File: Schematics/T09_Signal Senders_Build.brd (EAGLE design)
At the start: 88.6 x 64.8 mm, 39 parts, among them IC1 7805TV, IC2 7805TV, IC3 ATMEGA328, SW1 , X1 , Y2 16MHz

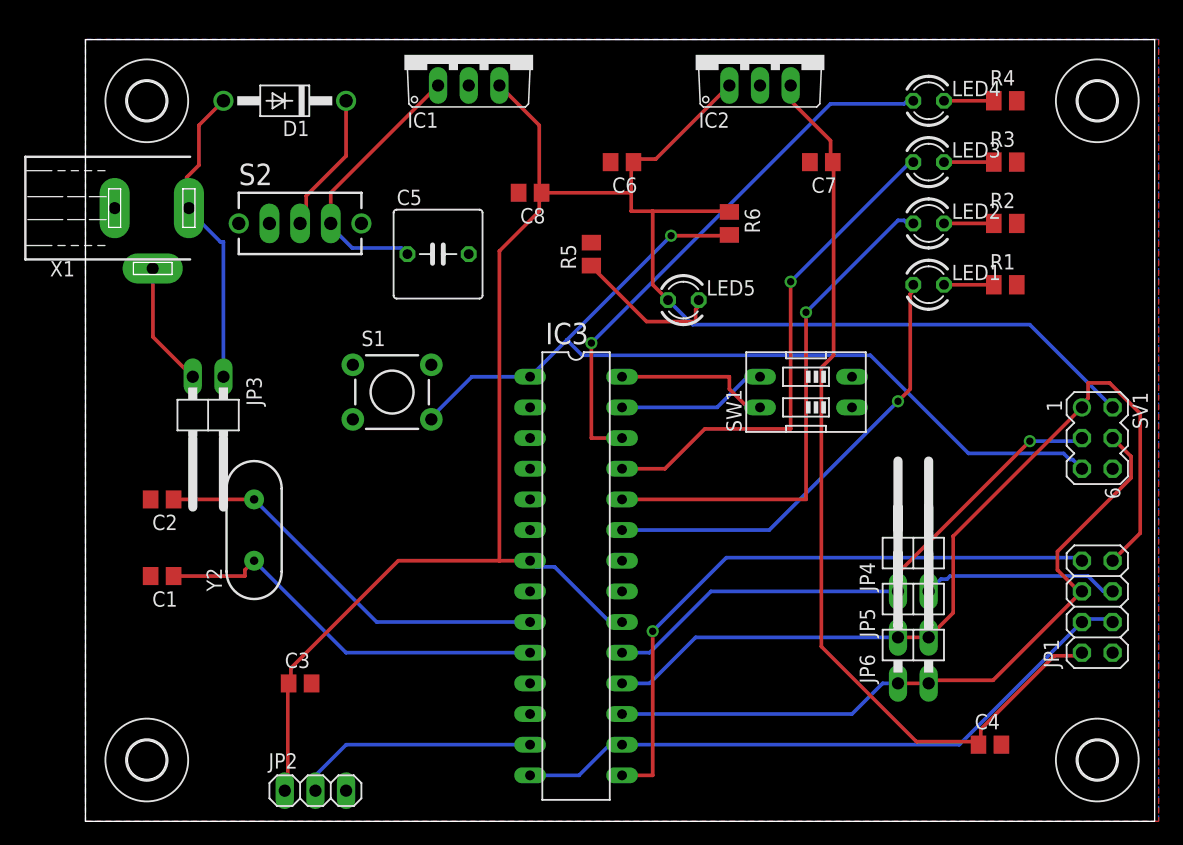
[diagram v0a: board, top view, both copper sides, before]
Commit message: PCB - added vias, added headers to uC unused pins
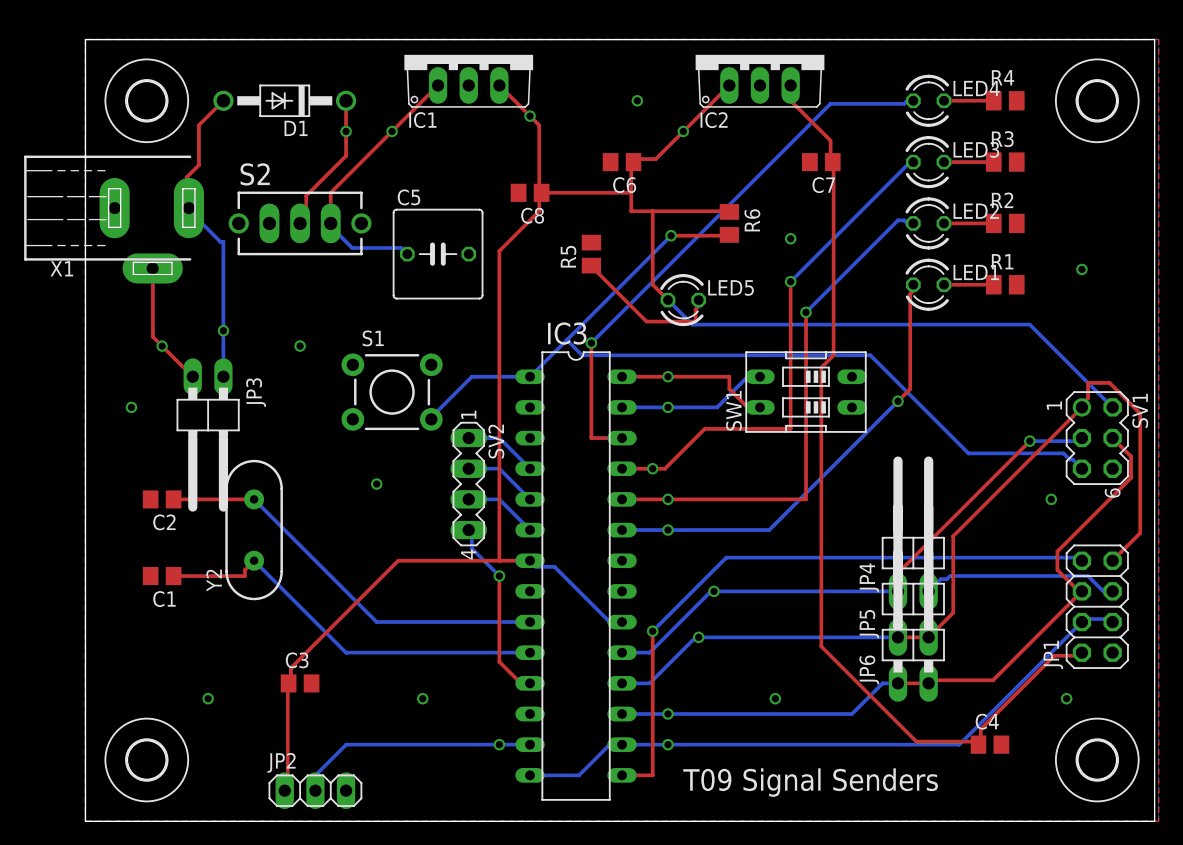
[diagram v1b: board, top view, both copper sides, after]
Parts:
- added SV2: (no value), con-lstb:MA04-1
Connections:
- net N$11: now also SV2.1
- net N$12: now also SV2.2
- net N$15: now also SV2.3
- net N$16: now also SV2.4
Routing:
- net N$16: track 0.00 -> 15.5 mm, vias 0 -> 1
- net N$15: track 0.00 -> 6.13 mm
- net N$12: track 0.00 -> 6.13 mm
- net N$11: track 0.00 -> 6.13 mm
- net N$14: vias 0 -> 1
- net SPI_CE: vias 0 -> 1
- net RF_SPIDSCSC: vias 0 -> 1
- net RF_SPIDSCS: vias 0 -> 1
- net RF_SPI5: vias 1 -> 2
- net N$9: vias 0 -> 1
- net N$4: vias 0 -> 1
- net N$23: vias 0 -> 1
- net N$22: vias 0 -> 1
- net N$10: vias 0 -> 1
- net LED2: vias 1 -> 2
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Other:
- board text added: "Chris Klupenger Max Cope Leslie Eide"
- board text added: "T09 Signal Senders"

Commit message: Fixed Nets. Fixed Silkscreen Layer
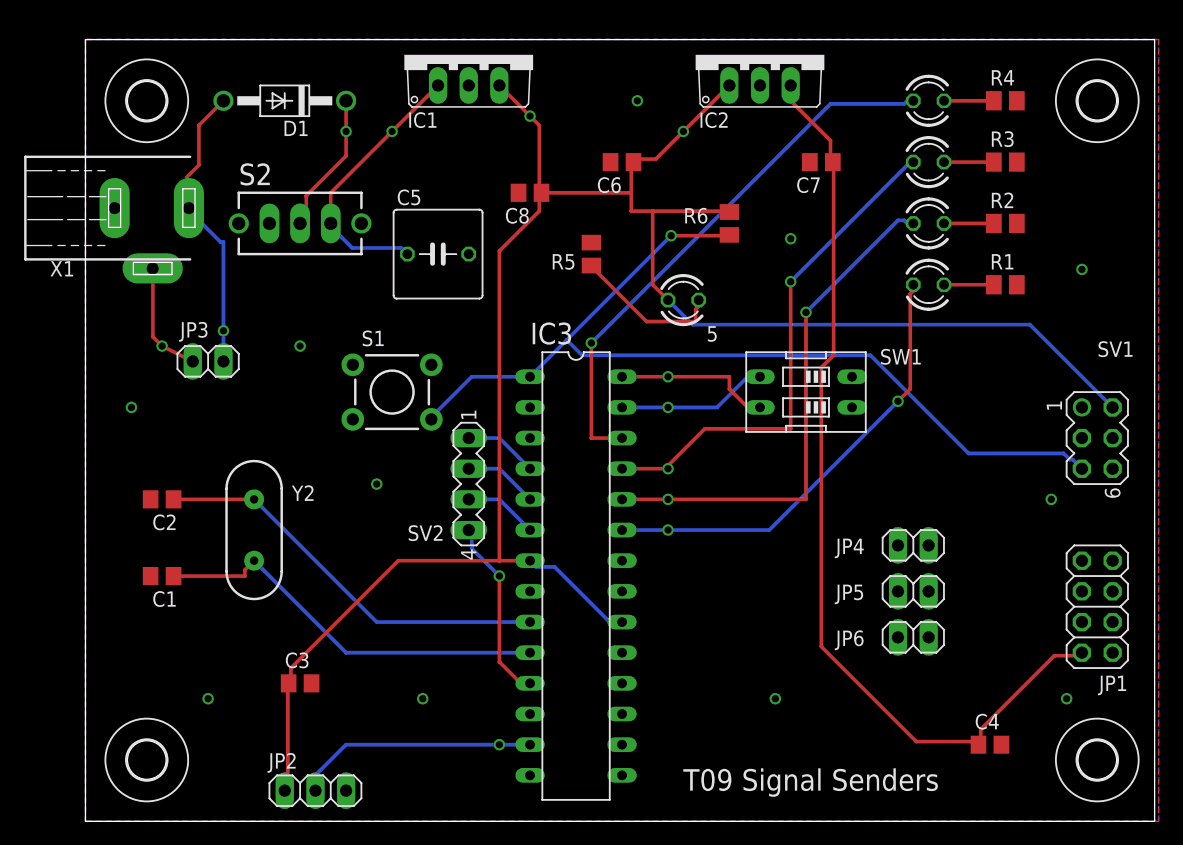
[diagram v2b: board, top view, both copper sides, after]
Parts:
- 5: value RED -> POWER
- JP1: value (none) -> RF
- JP2: value (none) -> IR
- JP3: value (none) -> Battery; device pinhead:1X02/90 -> pinhead:1X02
- JP4, JP5, JP6: device pinhead:1X02/90 -> pinhead:1X02
- LED1: value RED -> WEST
- LED2: value GREEN -> EAST
- LED3: value YELLOW -> SOUTH
- LED4: value BLUE -> NORTH
- S2: value TL32YO -> POWER
- SV1: value (none) -> SPI
- SW1: value (none) -> UNIT_ID
- moved JP3 5.08 mm to (10.2, 38.1)
- renumbered LED5 to 5
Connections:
- net RF_SPDSCSC renamed N$35
- net RF_SPI5 renamed N$33
- net RF_SPIDSCSD renamed N$39
- removed net RF_SPIDSCS: IC3.18, JP1.7, JP5.1, JP5.2, SV1.1
- removed net RF_SPIDSCSC: IC3.17, JP1.6, JP6.1, JP6.2, SV1.4
- removed net SPI_CE: IC3.14, IC3.16, JP1.3, JP1.4
- new net N$31: IC3.17, IC3.18, JP5.1, JP6.1, SV1.1, SV1.4
- new net N$34: IC3.14, JP1.4
- new net N$36: IC3.16, JP1.3
- new net N$37: JP1.6, JP6.2
- new net N$38: JP1.7, JP5.2
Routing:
- net RF_SPIDSCS: track 72.0 -> 0.00 mm, vias 1 -> 0
- net RF_SPIDSCSC: track 59.3 -> 0.00 mm, vias 1 -> 0
- net SPI_CE: track 53.7 -> 0.00 mm, vias 1 -> 0
- net N$35: track 52.7 -> 0.00 mm, vias 1 -> 0
- net N$33: track 46.4 -> 0.00 mm, vias 2 -> 0
- net N$39: track 16.3 -> 0.00 mm
- net +9V: track 25.9 -> 24.6 mm
- net N$14: track 10.3 -> 9.59 mm

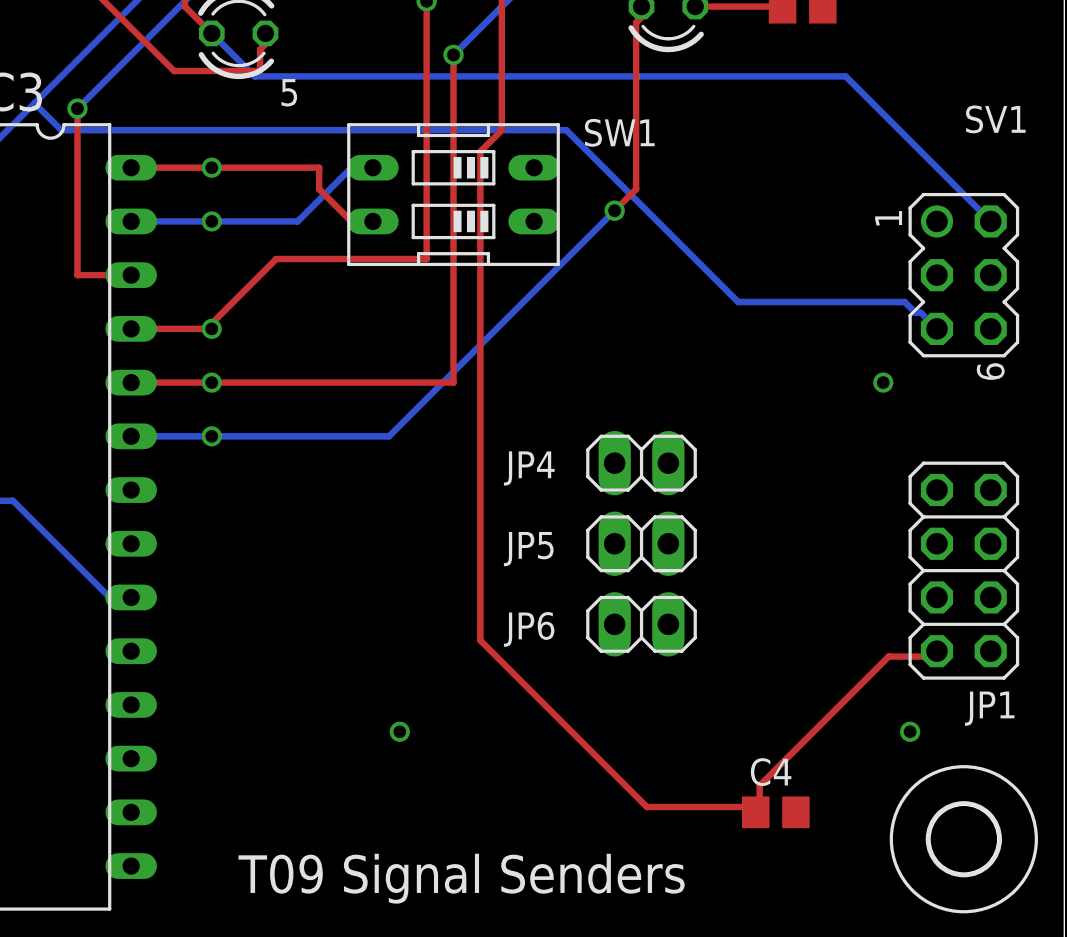
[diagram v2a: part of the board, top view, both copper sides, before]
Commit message: RF nets still had errors. Still need to be routed.
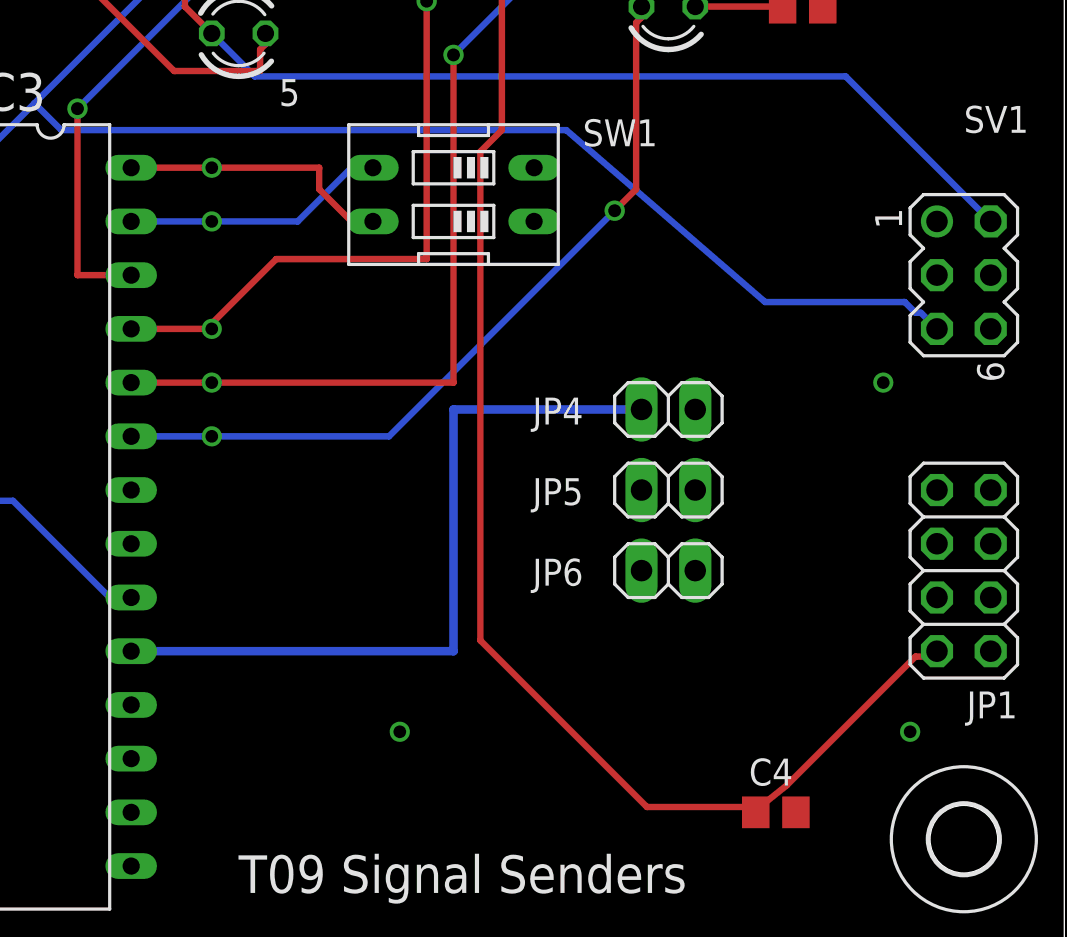
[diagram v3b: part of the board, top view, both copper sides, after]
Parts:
- SV2: value (none) -> (none)
- moved JP6 2.84 mm to (69.8, 17.8)
- moved JP4 2.84 mm to (69.8, 25.4)
- moved JP5 2.84 mm to (69.8, 21.6)
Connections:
- new net N$32: IC3.17, JP6.1, SV1.4
- net N$31: no longer IC3.17, JP6.1, SV1.4
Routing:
- net N$33: track 0.00 -> 35.6 mm
- net +3V3: track 77.9 -> 77.3 mm
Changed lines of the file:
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@@
 <attribute name="NAME" x="60.96" y="53.34" size="1.27" layer="25" rot="R180"/>
 </element>
-<element name="JP4" library="pinhead" package="1X02" value=" " x="68.58" y="22.86" smashed="yes">
-<attribute name="NAME" x="62.1538" y="22.1488" size="1.27" layer="25" ratio="10"/>
-<attribute name="VALUE" x="66.04" y="19.685" size="1.27" layer="27"/>
-</element>
-<element name="JP5" library="pinhead" package="1X02" value=" " x="68.58" y="19.05" smashed="yes">
-<attribute name="NAME" x="62.1538" y="18.3388" size="1.27" layer="25" ratio="10"/>
-<attribute name="VALUE" x="66.04" y="15.875" size="1.27" layer="27"/>
-</element>
-<element name="JP6" library="pinhead" package="1X02" value=" " x="68.58" y="15.24" smashed="yes">
-<attribute name="NAME" x="62.1538" y="14.5288" size="1.27" layer="25" ratio="10"/>
-<attribute name="VALUE" x="66.04" y="12.065" size="1.27" layer="27"/>
+<element name="JP4" library="pinhead" package="1X02" value=" " x="69.85" y="25.4" smashed="yes">
+<attribute name="NAME" x="63.4238" y="24.6888" size="1.27" layer="25" ratio="10"/>
+<attribute name="VALUE" x="67.31" y="22.225" size="1.27" layer="27"/>
+</element>
+<element name="JP5" library="pinhead" package="1X02" value=" " x="69.85" y="21.59" smashed="yes">
+<attribute name="NAME" x="63.4238" y="20.8788" size="1.27" layer="25" ratio="10"/>
+<attribute name="VALUE" x="67.31" y="18.415" size="1.27" layer="27"/>
+</element>
+<element name="JP6" library="pinhead" package="1X02" value=" " x="69.85" y="17.78" smashed="yes">
+<attribute name="NAME" x="63.4238" y="17.0688" size="1.27" layer="25" ratio="10"/>
+<attribute name="VALUE" x="67.31" y="14.605" size="1.27" layer="27"/>
 </element>
 <element name="R6" library="rcl" package="M0805" value="1k" x="53.34" y="49.53" smashed="yes" rot="R270">
@@
 <element name="U$3" library="holes" package="3,2" value="" x="83.82" y="59.69" smashed="yes"/>
 <element name="U$4" library="holes" package="3,2" value="" x="5.08" y="59.69" smashed="yes"/>
-<element name="SV2" library="con-lstb" package="MA04-1" value="" x="31.75" y="27.94" smashed="yes" rot="R270">
+<element name="SV2" library="con-lstb" package="MA04-1" value=" " x="31.75" y="27.94" smashed="yes" rot="R270">
 <attribute name="OC_NEWARK" value="unknown" x="31.75" y="27.94" size="1.778" layer="27" rot="R270" display="off"/>
 <attribute name="MPN" value="" x="31.75" y="27.94" size="1.778" layer="27" rot="R270" display="off"/>
@@
 <wire x1="81.534" y1="29.972" x2="81.788" y2="29.972" width="0.3048" layer="16"/>
 <wire x1="81.026" y1="30.48" x2="81.534" y2="29.972" width="0.3048" layer="16"/>
-<wire x1="73.152" y1="30.48" x2="81.026" y2="30.48" width="0.3048" layer="16"/>
-<wire x1="65.024" y1="38.608" x2="73.152" y2="30.48" width="0.3048" layer="16"/>
+<wire x1="74.422" y1="30.48" x2="81.026" y2="30.48" width="0.3048" layer="16"/>
+<wire x1="65.024" y1="38.608" x2="74.422" y2="30.48" width="0.3048" layer="16"/>
 <wire x1="41.148" y1="38.608" x2="65.024" y2="38.608" width="0.3048" layer="16"/>
 <wire x1="39.878" y1="39.878" x2="41.148" y2="38.608" width="0.3048" layer="16"/>
@@
 <wire x1="58.42" y1="60.96" x2="58.42" y2="59.69" width="0.3048" layer="1"/>
 <wire x1="61.722" y1="54.61" x2="61.91" y2="54.61" width="0.3048" layer="1"/>
-<wire x1="74.168" y1="7.62" x2="74.168" y2="6.604" width="0.3048" layer="1"/>
+<wire x1="75.438" y1="7.62" x2="74.168" y2="6.604" width="0.3048" layer="1"/>
 <wire x1="74.168" y1="6.604" x2="74.168" y2="6.35" width="0.3048" layer="1"/>
-<wire x1="80.264" y1="13.716" x2="74.168" y2="7.62" width="0.3048" layer="1"/>
-<wire x1="82.55" y1="13.716" x2="80.264" y2="13.716" width="0.3048" layer="1"/>
+<wire x1="81.534" y1="13.716" x2="75.438" y2="7.62" width="0.3048" layer="1"/>
+<wire x1="82.55" y1="13.716" x2="81.534" y2="13.716" width="0.3048" layer="1"/>
 <wire x1="82.55" y1="13.97" x2="82.55" y2="13.716" width="0.3048" layer="1"/>
 <wire x1="74.168" y1="6.35" x2="73.98" y2="6.35" width="0.3048" layer="1"/>
@@
 <via x="58.42" y="48.26" extent="1-16" drill="0.6"/>
 </signal>
-<signal name="N$31">
-<contactref element="IC3" pad="17"/>
-<contactref element="SV1" pad="4"/>
-<contactref element="JP6" pad="1"/>
-<contactref element="IC3" pad="18"/>
-<contactref element="SV1" pad="1"/>
-<contactref element="JP5" pad="1"/>
-<wire x1="82.55" y1="34.29" x2="85.09" y2="31.75" width="0" layer="19" extent="1-1"/>
-<wire x1="67.31" y1="19.05" x2="85.09" y2="31.75" width="0" layer="19" extent="1-1"/>
-<wire x1="67.31" y1="15.24" x2="67.31" y2="19.05" width="0" layer="19" extent="1-1"/>
-<wire x1="44.45" y1="11.43" x2="67.31" y2="15.24" width="0" layer="19" extent="1-1"/>
-<wire x1="44.45" y1="8.89" x2="44.45" y2="11.43" width="0" layer="19" extent="1-1"/>
-</signal>
 <signal name="N$33">
 <contactref element="IC3" pad="19"/>
 <contactref element="SV1" pad="3"/>
 <contactref element="JP4" pad="1"/>
-<wire x1="67.31" y1="22.86" x2="82.55" y2="31.75" width="0" layer="19" extent="1-1"/>
-<wire x1="44.45" y1="13.97" x2="67.31" y2="22.86" width="0" layer="19" extent="1-1"/>
+<wire x1="68.58" y1="25.4" x2="82.55" y2="31.75" width="0" layer="19" extent="1-1"/>
+<wire x1="44.45" y1="13.97" x2="68.58" y2="25.4" width="0" layer="19" extent="1-1"/>
+<wire x1="44.45" y1="13.97" x2="59.69" y2="13.97" width="0.4064" layer="16"/>
+<wire x1="59.69" y1="13.97" x2="59.69" y2="25.4" width="0.4064" layer="16"/>
+<wire x1="59.69" y1="25.4" x2="68.58" y2="25.4" width="0.4064" layer="16"/>
 </signal>
 <signal name="N$34">
@@
 <contactref element="JP6" pad="2"/>
 <contactref element="JP1" pad="6"/>
-<wire x1="69.85" y1="15.24" x2="82.55" y2="19.05" width="0" layer="19" extent="1-1"/>
+<wire x1="71.12" y1="17.78" x2="82.55" y2="19.05" width="0" layer="19" extent="1-1"/>
 </signal>
 <signal name="N$38">
 <contactref element="JP5" pad="2"/>
 <contactref element="JP1" pad="7"/>
-<wire x1="69.85" y1="19.05" x2="85.09" y2="21.59" width="0" layer="19" extent="1-1"/>
+<wire x1="71.12" y1="21.59" x2="85.09" y2="21.59" width="0" layer="19" extent="1-1"/>
 </signal>
 <signal name="N$39">
 <contactref element="JP4" pad="2"/>
 <contactref element="JP1" pad="5"/>
-<wire x1="69.85" y1="22.86" x2="85.09" y2="19.05" width="0" layer="19" extent="1-1"/>
+<wire x1="71.12" y1="25.4" x2="85.09" y2="19.05" width="0" layer="19" extent="1-1"/>
+</signal>
+<signal name="N$31">
+<contactref element="IC3" pad="18"/>
+<contactref element="SV1" pad="1"/>
+<contactref element="JP5" pad="1"/>
+<wire x1="68.58" y1="21.59" x2="82.55" y2="34.29" width="0" layer="19" extent="1-1"/>
+<wire x1="44.45" y1="11.43" x2="68.58" y2="21.59" width="0" layer="19" extent="1-1"/>
+</signal>
+<signal name="N$32">
+<contactref element="IC3" pad="17"/>
+<contactref element="SV1" pad="4"/>
+<contactref element="JP6" pad="1"/>
+<wire x1="68.58" y1="17.78" x2="85.09" y2="31.75" width="0" layer="19" extent="1-1"/>
+<wire x1="44.45" y1="8.89" x2="68.58" y2="17.78" width="0" layer="19" extent="1-1"/>
 </signal>
 </signals>
